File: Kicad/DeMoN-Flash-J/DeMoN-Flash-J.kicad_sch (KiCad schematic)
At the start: 37 parts, among them CN1 ECC43DCAI-S189, Q1 ZVP2106A, Q2 ZVP2106A, SW1 SW_Push, SW2 SW_Wuerth_450301014042, U1 GAL16V8, U10 IS61C5128AS-25QLI, U11 MC1455B, U2 GAL16V8, U3 GAL16V8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

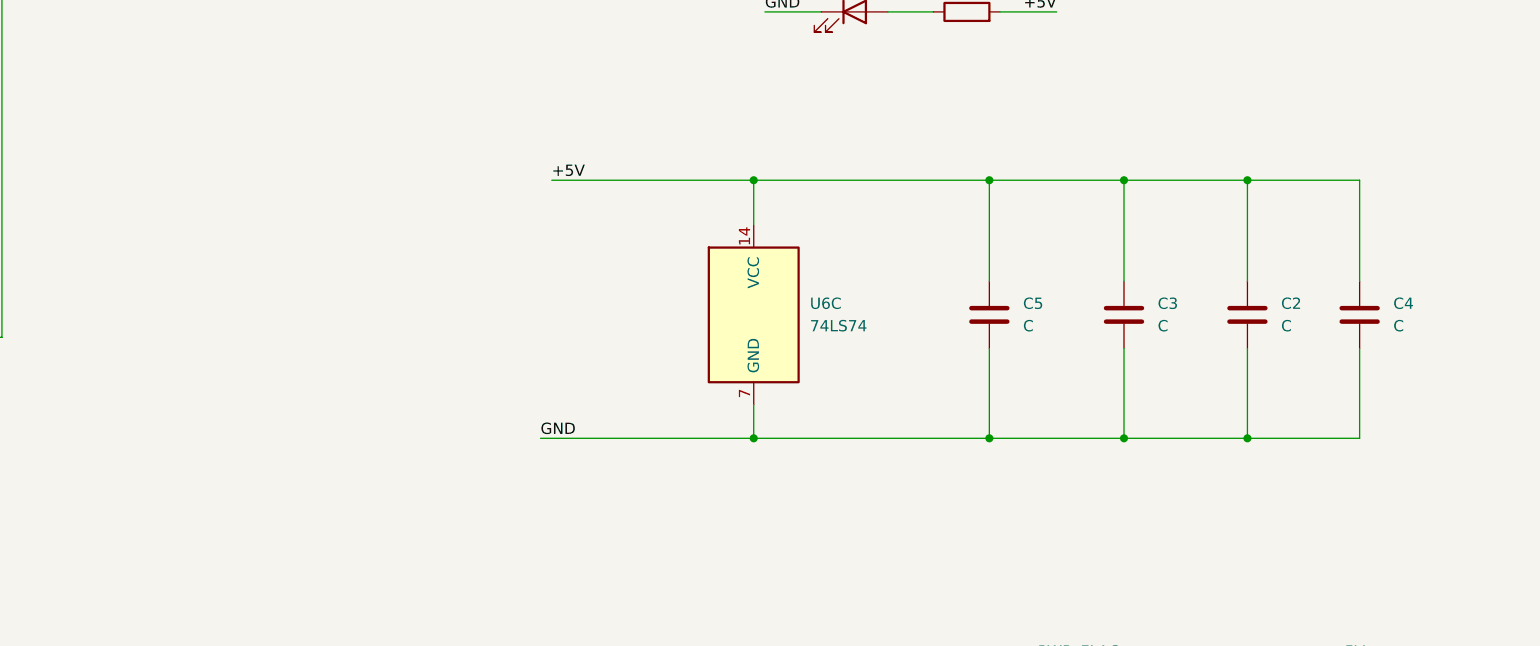
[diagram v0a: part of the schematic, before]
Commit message: added some decoupling cap
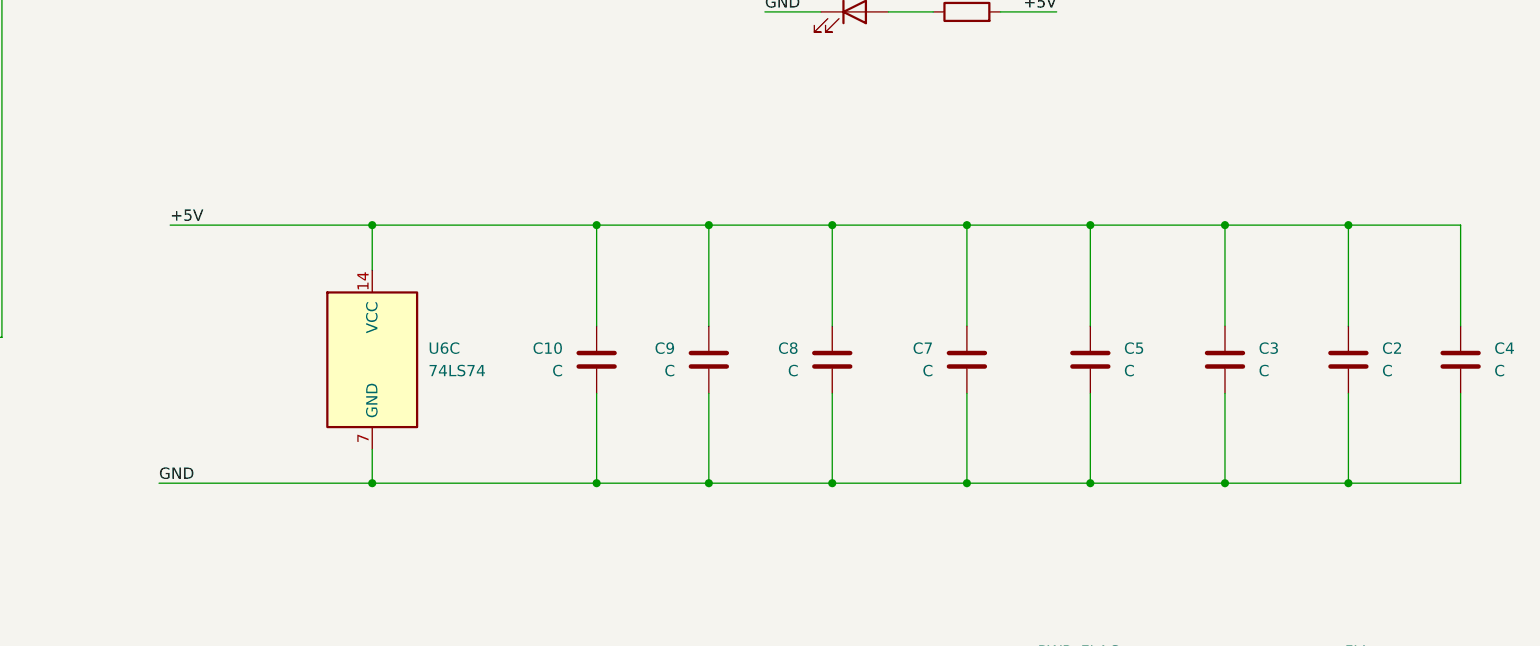
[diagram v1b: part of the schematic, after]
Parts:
- added C10, C7, C8, C9: C, Capacitor_SMD:C_1206_3216Metric_Pad1.33x1.80mm_HandSolder, symbol Device:C
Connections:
- net +5V: now also C10.2, C7.1, C8.1, C9.1
- net GND: now also C10.1, C7.2, C8.2, C9.2
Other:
- moved on the sheet: C2, C3, C4, C5, U6C

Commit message: Bigger PLCC pads for easier handsoldering
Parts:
- U1, U2, U3, U4, U5: footprint Package_LCC:PLCC-20 -> ARIII_Shared:PLCC-20-Handsoldering
